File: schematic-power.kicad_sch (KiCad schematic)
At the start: 30 parts, among them U4 TPS62933, U9 TPS62933

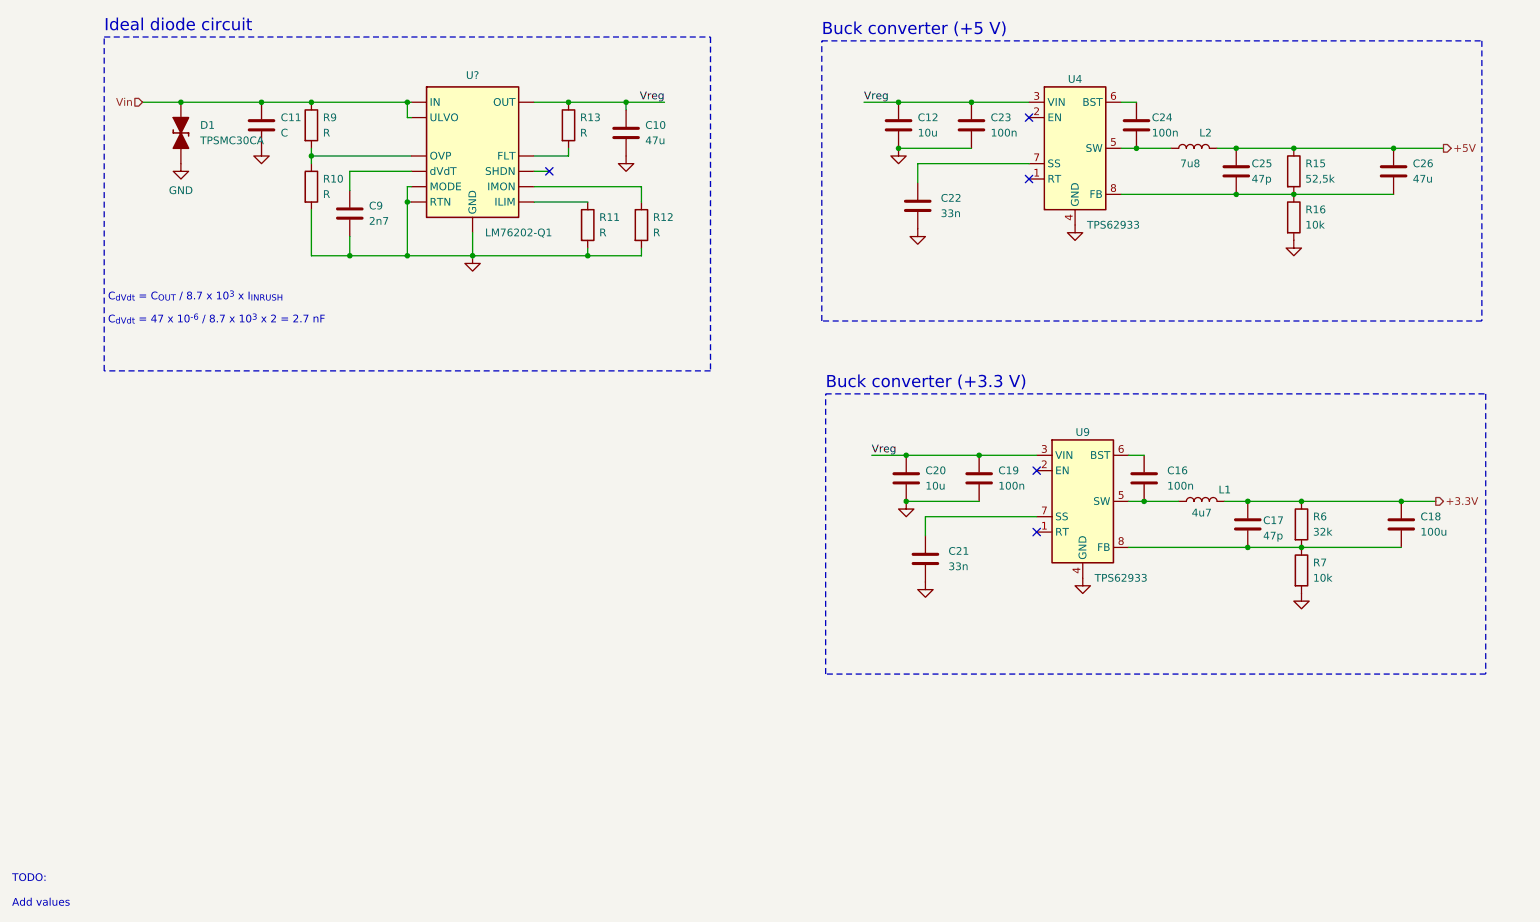
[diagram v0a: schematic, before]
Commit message: Redesign schematic structure using hierarchical sheets
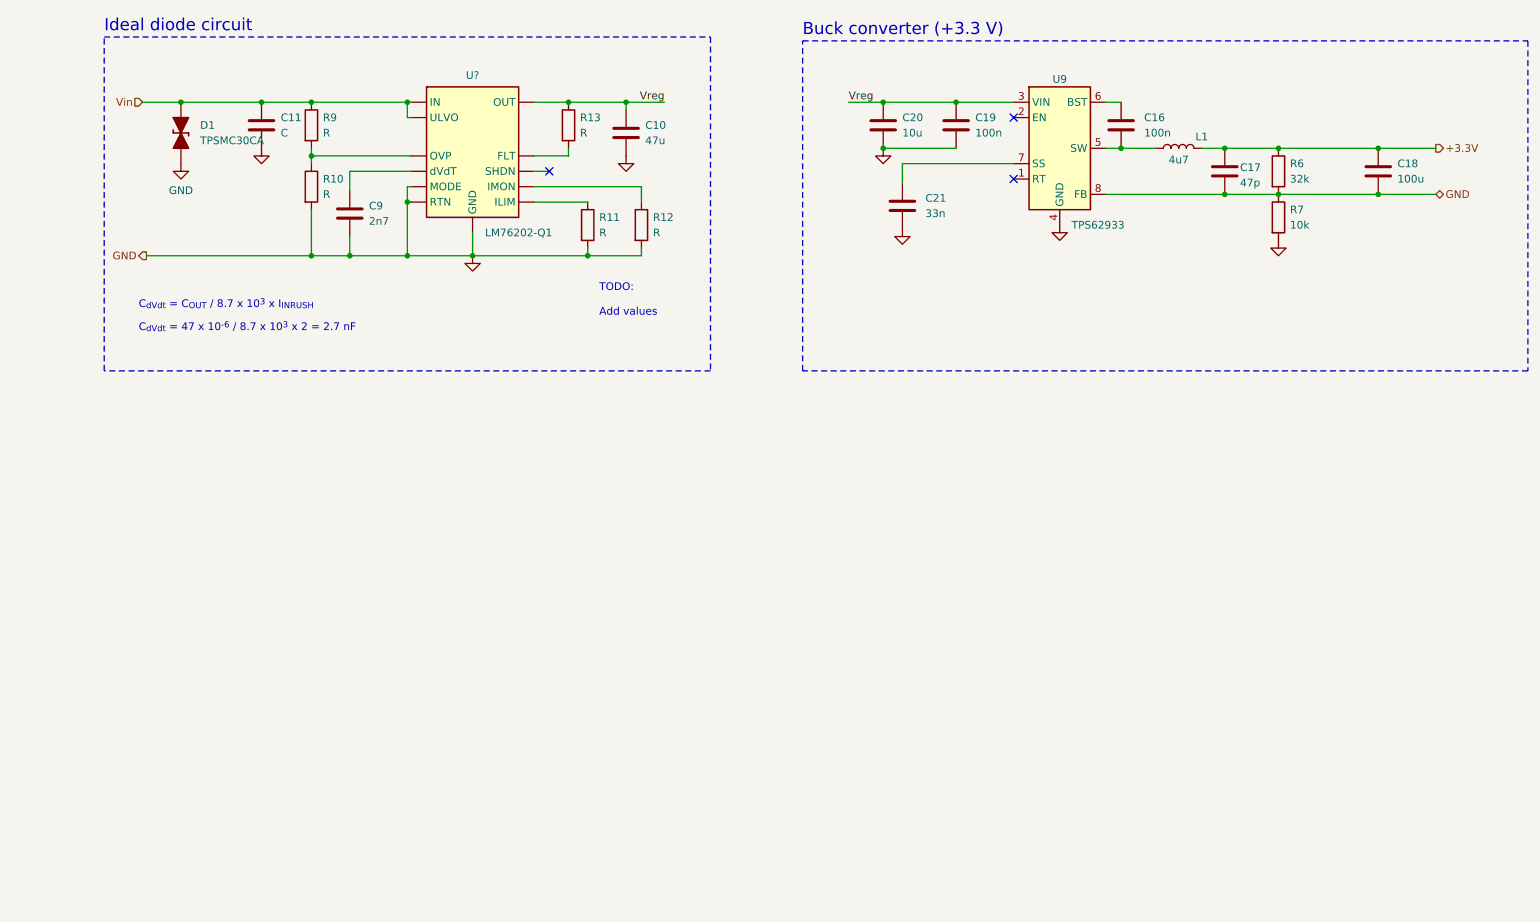
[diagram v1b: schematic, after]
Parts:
- removed C12: 10u, symbol Device:C
- removed C22: 33n, symbol Device:C
- removed C23, C24: 100n, symbol Device:C
- removed C25: 47p, symbol Device:C
- removed C26: 47u, symbol Device:C
- removed L2: 7u8, symbol Device:L
- removed R15: 52,5k, symbol Device:R
- removed R16: 10k, symbol Device:R
- removed U4: TPS62933, Package_TO_SOT_SMD:SOT-583-8, symbol Regulator_Switching:TPS62933
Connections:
- net GND: now also C17.2, C18.2, R6.2, R7.1, U9.8 (FB)
- no-connect marks 5 -> 3
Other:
- note removed: "Buck converter (+5 V)"
- moved on the sheet: C16, C17, C18, C19, C20, C21, L1, R6, R7, U9

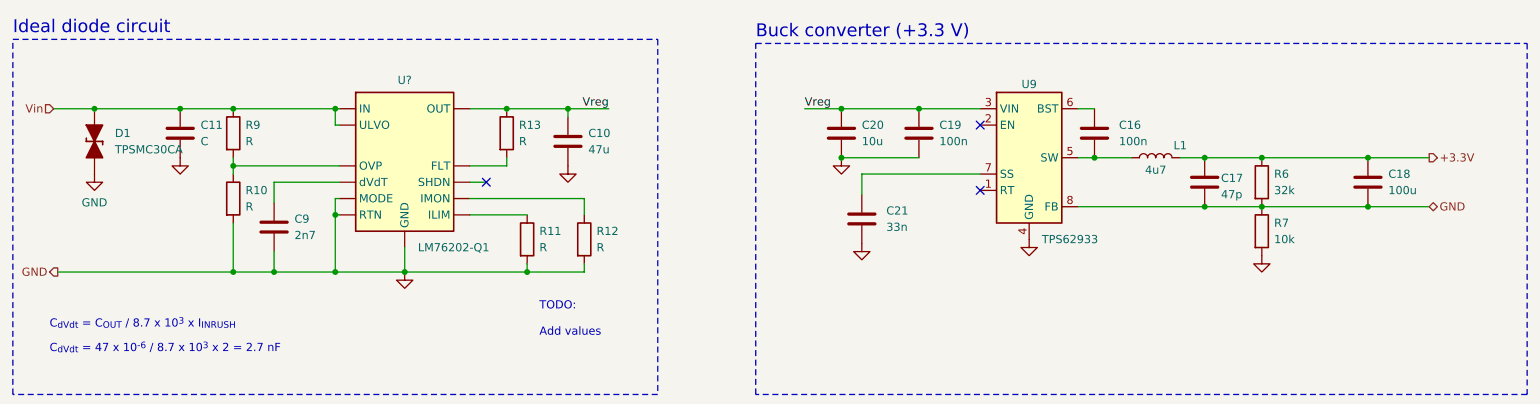
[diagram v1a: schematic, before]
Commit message: Fix most issues with found after ERC
Grid size, unconnected ping, PWR_FLAGs
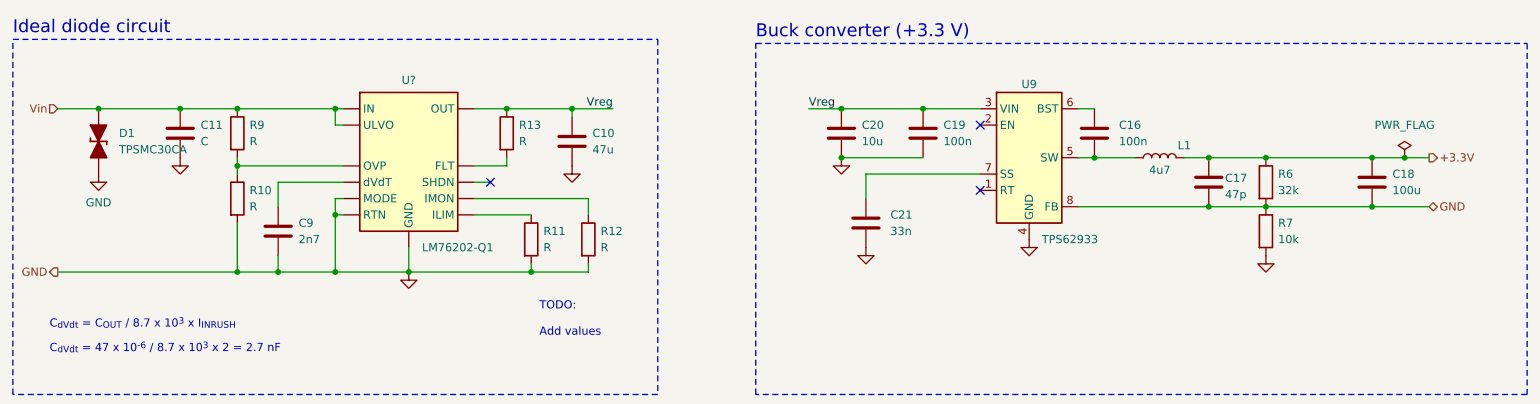
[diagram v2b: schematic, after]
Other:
- company: (none) -> Hydrogreen Pollub
- title: (none) -> Motor driver unit
- moved on the sheet: C10, C17, C18, C19, C21, C9, D1, L1, R10, R11, R12, R6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

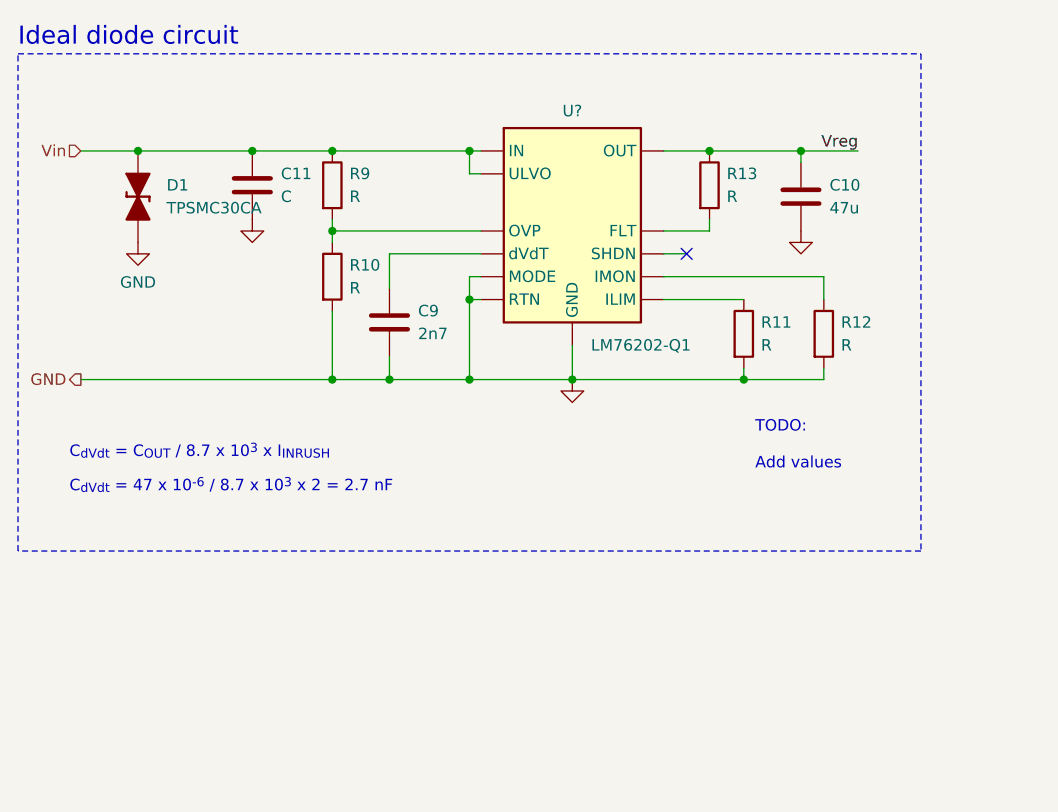
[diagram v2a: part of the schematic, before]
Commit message: Add values for ideal diode circuit
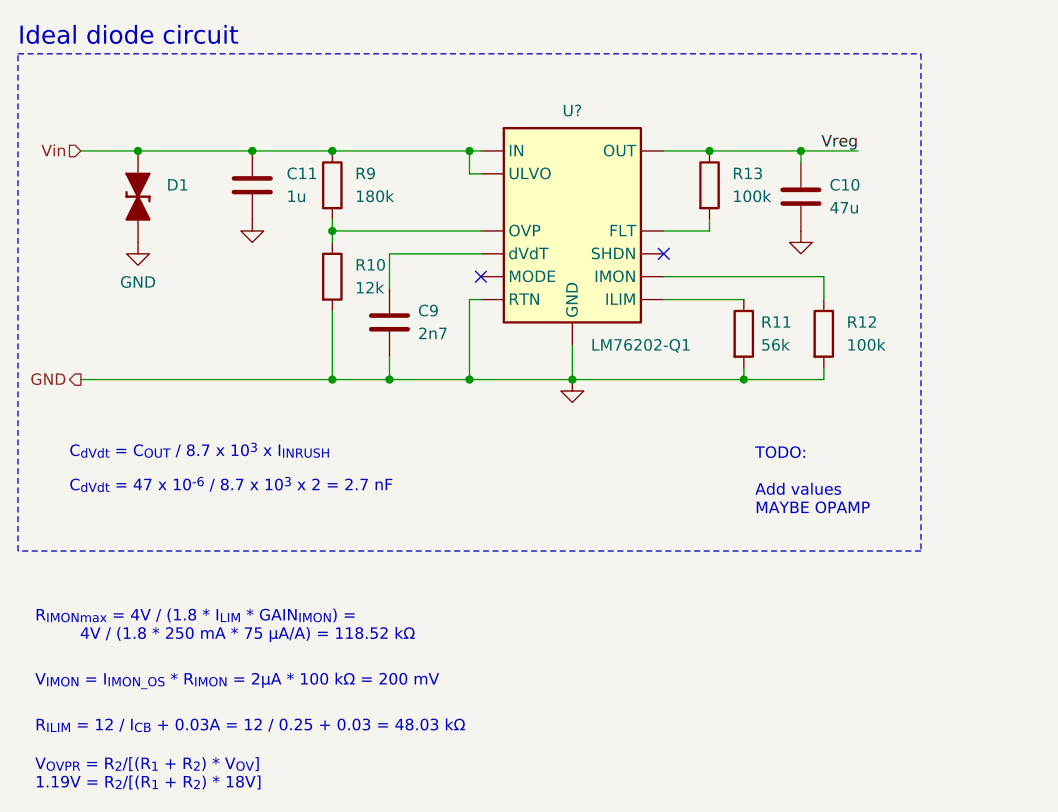
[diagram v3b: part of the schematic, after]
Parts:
- C11: value C -> 1u
- R10: value R -> 12k
- R11: value R -> 56k
- R12, R13: value R -> 100k
- R9: value R -> 180k
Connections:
- no-connect marks 3 -> 4
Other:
- note added: "R_{ILIM} = 12 / I_{CB} + 0.03A = 12 / 0.25 + 0.03 = 48.03 kΩ"
- note added: "R_{IMONmax} = 4V / (1.8 * I_{LIM} * GAIN_{IMON}) = 4V / (1.8 * 250 mA * 75 µA/A) = 118.52 kΩ"
- note added: "TODO: Add values MAYBE OPAMP"
- note added: "V_{IMON} = I_{IMON_OS} * R_{IMON} = 2µA * 100 kΩ = 200 mV"
- note added: "V_{OVPR} = R_{2}/[(R_{1} + R_{2}) * V_{OV}] 1.19V = R_{2}/[(R_{1} + R_{2}) * 18V]"
- note removed: "TODO: Add values"
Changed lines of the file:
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@@
   (junction (at 242.57 68.58) (diameter 0) (color 0 0 0 0)
   )
-  (junction (at 81.28 77.47) (diameter 0) (color 0 0 0 0)
-  )
   (junction (at 118.11 60.96) (diameter 0) (color 0 0 0 0)
   )
   (junction (at 172.72 60.96) (diameter 0) (color 0 0 0 0)
   )
-  (no_connect (at 105.41 72.39))
+  (no_connect (at 82.55 74.93))
+  (no_connect (at 102.87 72.39))
   (no_connect (at 181.61 73.66))
   (no_connect (at 181.61 63.5))
@@
     (stroke (width 0) (type default))
   )
-  (wire (pts (xy 81.28 74.93) (xy 81.28 77.47))
-    (stroke (width 0) (type default))
-  )
   (wire (pts (xy 66.04 69.85) (xy 66.04 71.12))
     (stroke (width 0) (type default))
@@
     (stroke (width 0) (type default))
   )
-  (wire (pts (xy 105.41 72.39) (xy 102.87 72.39))
-    (stroke (width 0) (type default))
-  )
   (wire (pts (xy 66.04 68.58) (xy 66.04 69.85))
     (stroke (width 0) (type default))
@@
   )
   (wire (pts (xy 120.65 77.47) (xy 120.65 74.93))
-    (stroke (width 0) (type default))
-  )
-  (wire (pts (xy 81.28 74.93) (xy 82.55 74.93))
     (stroke (width 0) (type default))
   )
@@
     (fill (type none))
   )
+  (text "V_{IMON} = I_{IMON_OS} * R_{IMON} = 2µA * 100 kΩ = 200 mV"
+    (at 33.02 120.65 0)
+    (effects (font (size 1.27 1.27)) (justify left bottom))
+  )
   (text "C_{dVdt} = 47 x 10^{-6} / 8.7 x 10^{3} x 2 = 2.7 nF"
     (at 36.83 99.06 0)
@@
     (effects (font (size 1.27 1.27)) (justify left bottom))
   )
+  (text "V_{OVPR} = R_{2}/[(R_{1} + R_{2}) * V_{OV}]\n1.19V = R_{2}/[(R_{1} + R_{2}) * 18V]"
+    (at 33.02 132.08 0)
+    (effects (font (size 1.27 1.27)) (justify left bottom))
+  )
+  (text "R_{IMONmax} = 4V / (1.8 * I_{LIM} * GAIN_{IMON}) =\n	 	4V / (1.8 * 250 mA * 75 µA/A) = 118.52 kΩ"
+    (at 33.02 115.57 0)
+    (effects (font (size 1.27 1.27)) (justify left bottom))
+  )
+  (text "R_{ILIM} = 12 / I_{CB} + 0.03A = 12 / 0.25 + 0.03 = 48.03 kΩ"
+    (at 33.02 125.73 0)
+    (effects (font (size 1.27 1.27)) (justify left bottom))
+  )
   (text "Ideal diode circuit\n" (at 31.115 49.53 0)
     (effects (font (size 2 2)) (justify left bottom))
@@
     (effects (font (size 2 2)) (justify left bottom))
   )
-  (text "TODO:\n\nAdd values" (at 113.03 96.52 0)
+  (text "TODO:\n\nAdd values\nMAYBE OPAMP" (at 113.03 101.6 0)
     (effects (font (size 1.27 1.27)) (justify left bottom))
   )
@@
   (symbol (lib_id "Device:C") (at 57.15 64.77 0) (unit 1)
     (in_bom yes) (on_board yes) (dnp no) (fields_autoplaced)
-    (property "Reference" "C11" (at 60.325 63.4999 0)
-      (effects (font (size 1.27 1.27)) (justify left))
-    )
-    (property "Value" "C" (at 60.325 66.0399 0)
+    (property "Reference" "C11" (at 60.96 63.5 0)
+      (effects (font (size 1.27 1.27)) (justify left))
+    )
+    (property "Value" "1u" (at 60.96 66.04 0)
       (effects (font (size 1.27 1.27)) (justify left))
     )
@@
       (effects (font (size 1.27 1.27)) hide)
     )
-    (property "Datasheet" "" (at 96.52 58.42 0)
+    (property "Datasheet" "https://www.ti.com/lit/ds/symlink/lm76202-q1.pdf?ts=1699938980962&ref_url=https%253A%252F%252Fwww.ti.com%252Fsitesearch%252Fen-us%252Fdocs%252Funiversalsearch.tsp%253FlangPref%253Den-US%2526searchTerm%253Dideal%2Bdiode%2526nr%253D11691" (at 96.52 58.42 0)
       (effects (font (size 1.27 1.27)) hide)
     )
@@
   (symbol (lib_id "Device:R") (at 107.95 64.77 0) (unit 1)
     (in_bom yes) (on_board yes) (dnp no) (fields_autoplaced)
-    (property "Reference" "R13" (at 109.855 63.4999 0)
-      (effects (font (size 1.27 1.27)) (justify left))
-    )
-    (property "Value" "R" (at 109.855 66.0399 0)
+    (property "Reference" "R13" (at 110.49 63.5 0)
+      (effects (font (size 1.27 1.27)) (justify left))
+    )
+    (property "Value" "100k" (at 110.49 66.04 0)
       (effects (font (size 1.27 1.27)) (justify left))
     )
@@
   (symbol (lib_id "Device:R") (at 120.65 81.28 0) (unit 1)
     (in_bom yes) (on_board yes) (dnp no) (fields_autoplaced)
-    (property "Reference" "R12" (at 122.555 80.0099 0)
-      (effects (font (size 1.27 1.27)) (justify left))
-    )
-    (property "Value" "R" (at 122.555 82.5499 0)
+    (property "Reference" "R12" (at 123.19 80.01 0)
+      (effects (font (size 1.27 1.27)) (justify left))
+    )
+    (property "Value" "100k" (at 123.19 82.55 0)
       (effects (font (size 1.27 1.27)) (justify left))
     )
@@
     )
     (property "Value" "TPSMC30CA" (at 47.625 67.3099 90)
-      (effects (font (size 1.27 1.27)) (justify right))
+      (effects (font (size 1.27 1.27)) (justify right) hide)
     )
     (property "Footprint" "Diode_SMD_AKL:D_SMC_TVS" (at 44.45 66.04 0)
@@
   (symbol (lib_id "Device:R") (at 66.04 64.77 0) (unit 1)
     (in_bom yes) (on_board yes) (dnp no) (fields_autoplaced)
-    (property "Reference" "R9" (at 67.945 63.4999 0)
-      (effects (font (size 1.27 1.27)) (justify left))
-    )
-    (property "Value" "R" (at 67.945 66.0399 0)
+    (property "Reference" "R9" (at 68.58 63.5 0)
+      (effects (font (size 1.27 1.27)) (justify left))
+    )
+    (property "Value" "180k" (at 68.58 66.04 0)
       (effects (font (size 1.27 1.27)) (justify left))
     )
@@
   (symbol (lib_id "Device:R") (at 66.04 74.93 0) (unit 1)
     (in_bom yes) (on_board yes) (dnp no) (fields_autoplaced)
-    (property "Reference" "R10" (at 67.945 73.6599 0)
-      (effects (font (size 1.27 1.27)) (justify left))
-    )
-    (property "Value" "R" (at 67.945 76.1999 0)
+    (property "Reference" "R10" (at 68.58 73.66 0)
+      (effects (font (size 1.27 1.27)) (justify left))
+    )
+    (property "Value" "12k" (at 68.58 76.2 0)
       (effects (font (size 1.27 1.27)) (justify left))
     )
@@
       (effects (font (size 1.27 1.27)) (justify left))
     )
-    (property "Value" "R" (at 113.665 82.5499 0)
-      (effects (font (size 1.27 1.27)) (justify left))
-    )
+    (property "Value" "56k" (at 113.665 82.5499 0)
+      (effects (font (size 1.27 1.27)) (justify left))
+    )

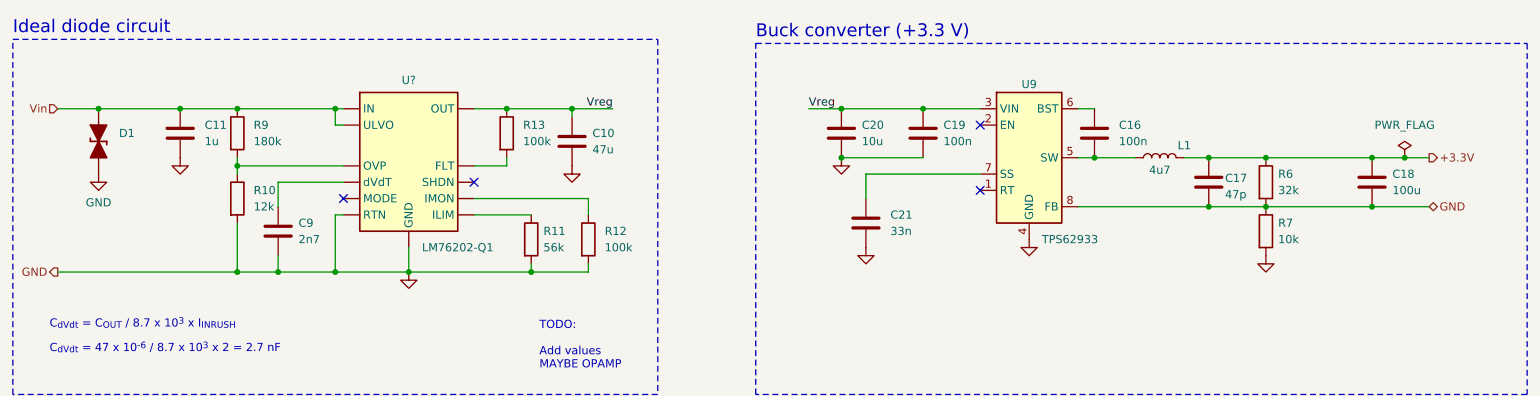
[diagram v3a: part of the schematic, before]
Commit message: Fix ERC checks related to hierarchical labels
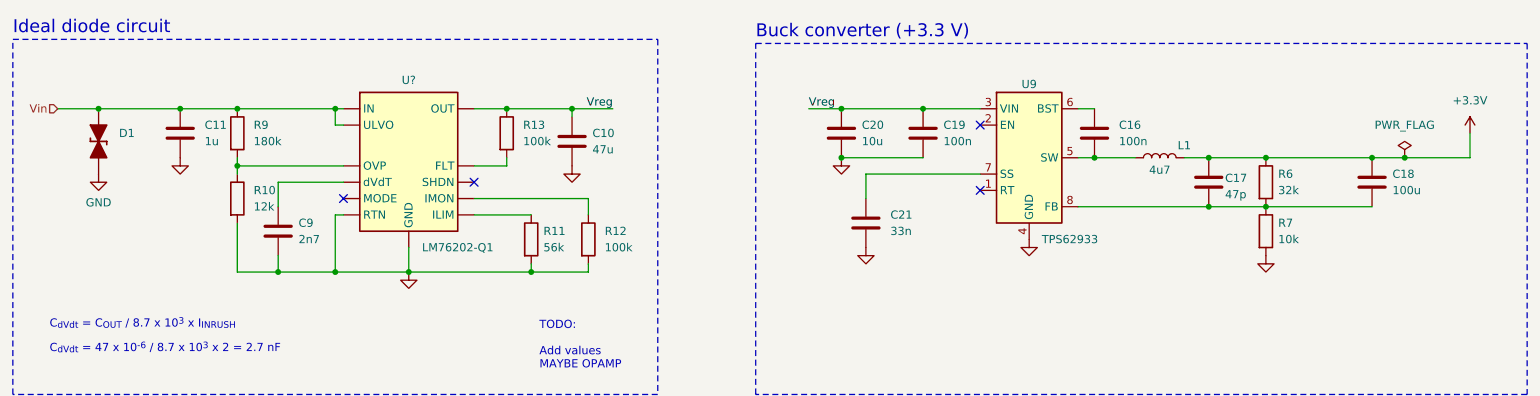
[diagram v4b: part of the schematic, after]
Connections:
- net GND: no longer C17.2, C18.2, R6.2, R7.1, U9.8 (FB)
- new net: C17.2, C18.2, R6.2, R7.1, U9.8 (FB)
